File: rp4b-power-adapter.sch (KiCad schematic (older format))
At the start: 6 parts, among them X1 TYPE-C-31-M-12, X2 FH-00339

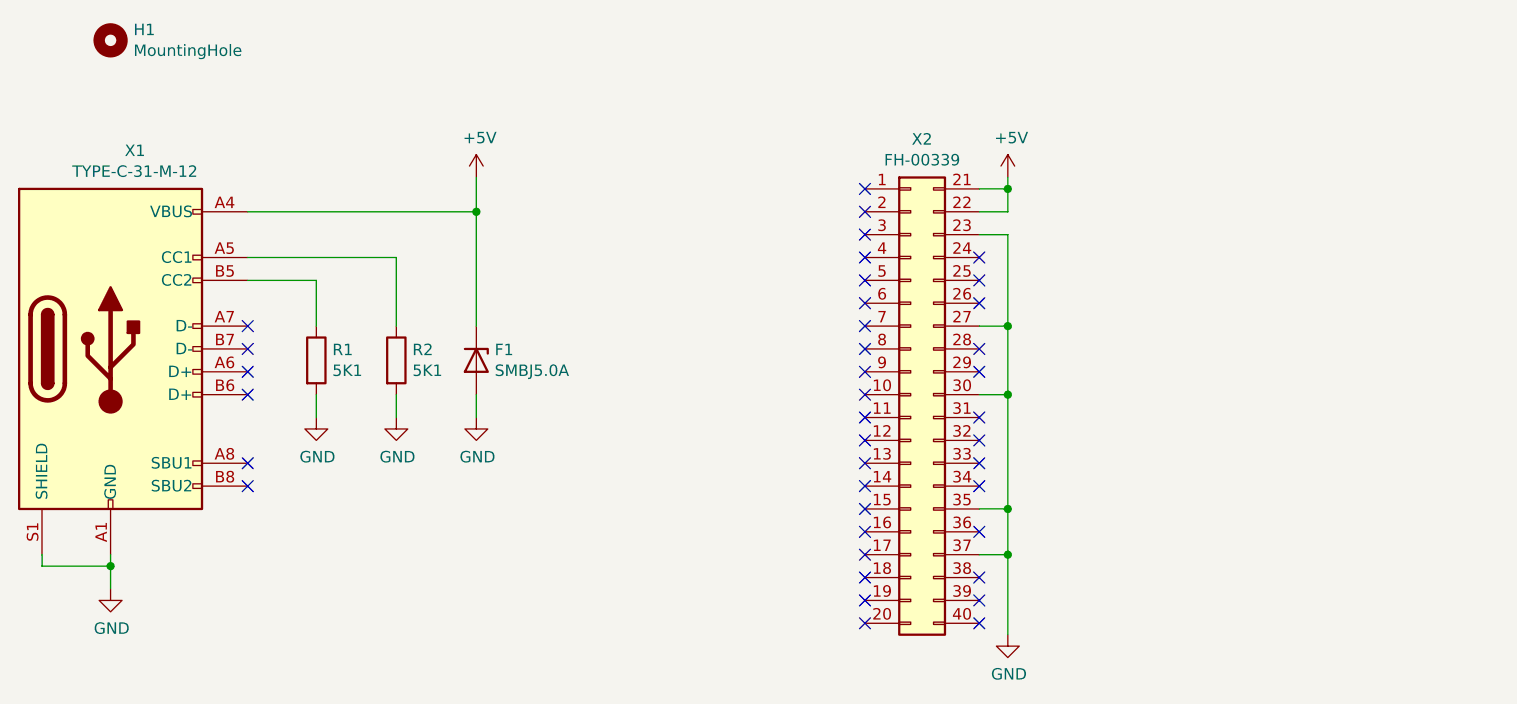
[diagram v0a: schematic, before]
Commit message: Add additional holes for FH-00369 and alternatives for FH-00339 (FH-00369, FH-00148)
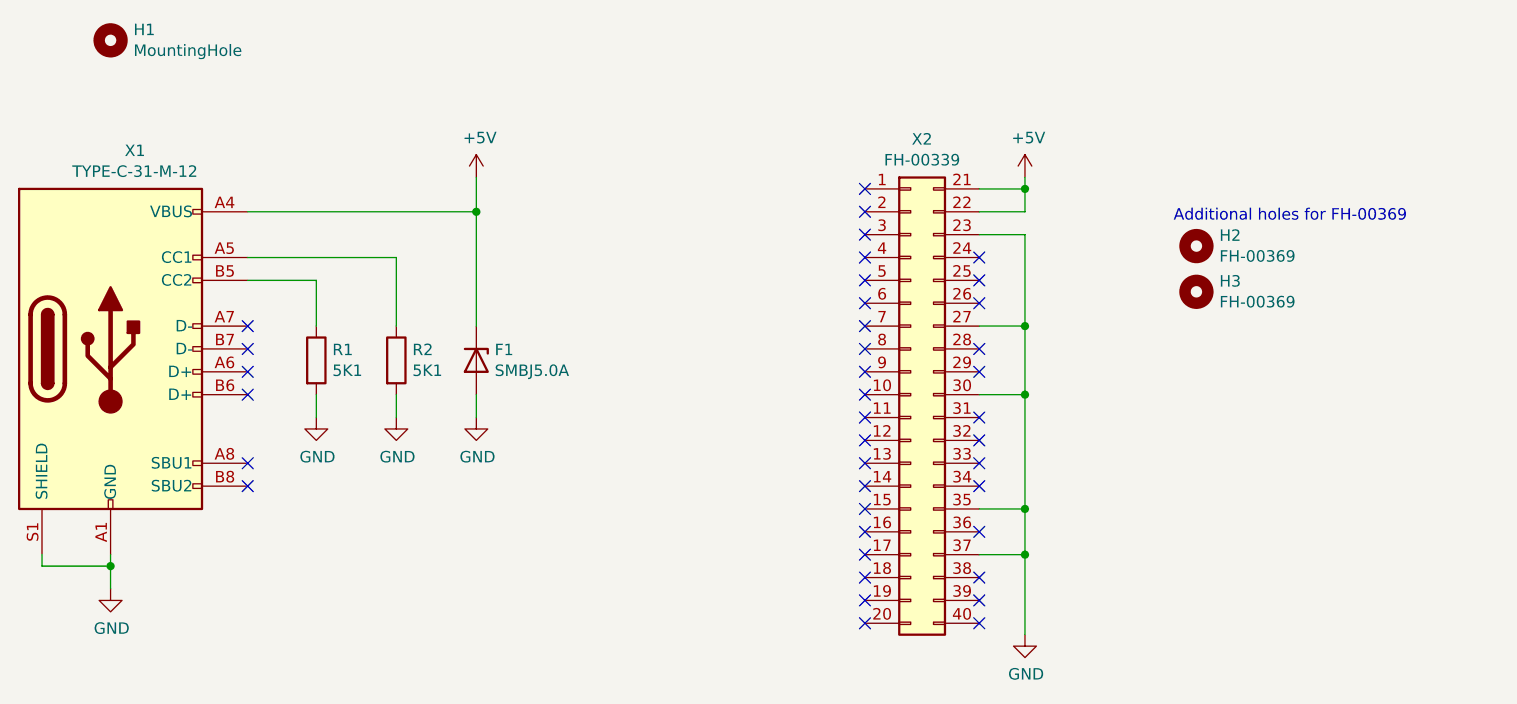
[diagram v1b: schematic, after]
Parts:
- added H2, H3: FH-00369, Hole:Hole_1.8mm, symbol Mechanical:MountingHole
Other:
- note added: "Additional holes for FH-00369"
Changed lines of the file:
@@
 L power:+5V #PWR0101
 U 1 1 61770C6A
-P 7975 2700
-F 0 "#PWR0101" H 7975 2550 50  0001 C CNN
-F 1 "+5V" H 7990 2873 50  0000 C CNN
-F 2 "" H 7975 2700 50  0001 C CNN
-F 3 "" H 7975 2700 50  0001 C CNN
-	1    7975 2700
+P 8050 2700
+F 0 "#PWR0101" H 8050 2550 50  0001 C CNN
+F 1 "+5V" H 8065 2873 50  0000 C CNN
+F 2 "" H 8050 2700 50  0001 C CNN
+F 3 "" H 8050 2700 50  0001 C CNN
+	1    8050 2700
 	1    0    0    -1
 $EndComp
@@
 L power:GND #PWR0102
 U 1 1 61771DD7
-P 7975 4700
-F 0 "#PWR0102" H 7975 4450 50  0001 C CNN
-F 1 "GND" H 7980 4527 50  0000 C CNN
-F 2 "" H 7975 4700 50  0001 C CNN
-F 3 "" H 7975 4700 50  0001 C CNN
-	1    7975 4700
+P 8050 4700
+F 0 "#PWR0102" H 8050 4450 50  0001 C CNN
+F 1 "GND" H 8055 4527 50  0000 C CNN
+F 2 "" H 8050 4700 50  0001 C CNN
+F 3 "" H 8050 4700 50  0001 C CNN
+	1    8050 4700
 	1    0    0    -1
 $EndComp
@@
 $EndComp
 Wire Wire Line
-	7975 2950 7975 3350
-Connection ~ 7975 3350
-Wire Wire Line
-	7975 3350 7975 3650
-Connection ~ 7975 3650
-Wire Wire Line
-	7975 3650 7975 4150
-Connection ~ 7975 4150
-Wire Wire Line
-	7975 4150 7975 4350
-Wire Wire Line
-	7975 4350 7975 4700
-Connection ~ 7975 4350
-Wire Wire Line
-	7975 2750 7975 2700
-Wire Wire Line
-	7975 2850 7975 2750
-Connection ~ 7975 2750
-Wire Wire Line
-	7850 2850 7975 2850
-Wire Wire Line
-	7850 2750 7975 2750
-Wire Wire Line
-	7850 2950 7975 2950
-Wire Wire Line
-	7850 3350 7975 3350
-Wire Wire Line
-	7850 3650 7975 3650
-Wire Wire Line
-	7850 4150 7975 4150
-Wire Wire Line
-	7850 4350 7975 4350
+	8050 2950 8050 3350
+Connection ~ 8050 3350
+Wire Wire Line
+	8050 3350 8050 3650
+Connection ~ 8050 3650
+Wire Wire Line
+	8050 3650 8050 4150
+Connection ~ 8050 4150
+Wire Wire Line
+	8050 4150 8050 4350
+Wire Wire Line
+	8050 4350 8050 4700
+Connection ~ 8050 4350
+Wire Wire Line
+	8050 2750 8050 2700
+Wire Wire Line
+	8050 2850 8050 2750
+Connection ~ 8050 2750
+Wire Wire Line
+	7850 2850 8050 2850
+Wire Wire Line
+	7850 2750 8050 2750
+Wire Wire Line
+	7850 2950 8050 2950
+Wire Wire Line
+	7850 3350 8050 3350
+Wire Wire Line
+	7850 3650 8050 3650
+Wire Wire Line
+	7850 4150 8050 4150
+Wire Wire Line
+	7850 4350 8050 4350
 NoConn ~ 7350 2750
 NoConn ~ 7350 2850
@@
 	1    0    0    -1
 $EndComp
+$Comp
+L Mechanical:MountingHole H2
+U 1 1 618FD732
+P 8800 3000
+F 0 "H2" H 8900 3046 50  0000 L CNN
+F 1 "FH-00369" H 8900 2955 50  0000 L CNN
+F 2 "Hole:Hole_1.8mm" H 8800 3000 50  0001 C CNN
+F 3 "~" H 8800 3000 50  0001 C CNN
+	1    8800 3000
+	1    0    0    -1
+$EndComp
+$Comp
+L Mechanical:MountingHole H3
+U 1 1 618FDB83
+P 8800 3200
+F 0 "H3" H 8900 3246 50  0000 L CNN
+F 1 "FH-00369" H 8900 3155 50  0000 L CNN
+F 2 "Hole:Hole_1.8mm" H 8800 3200 50  0001 C CNN
+F 3 "~" H 8800 3200 50  0001 C CNN
+	1    8800 3200
+	1    0    0    -1
+$EndComp
+Text Notes 8700 2900 0    50   ~ 0
+Additional holes for FH-00369
 $EndSCHEMATC
